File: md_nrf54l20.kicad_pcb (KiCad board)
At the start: 4 copper layers, 43.2 x 17.8 mm, 56 parts, among them J10 Conn_01x15, J2 Conn_01x04, J5 USB_C, J7 JST SH I2C, J9 Conn_01x15, SW1 RESET, U1 nRF54L20, U3 CH347T, U4 AP2112K-3.3, U5 MLD-TF PUSH-H18, U6 CH347F, Y1 8MHz, Y2 32MHz

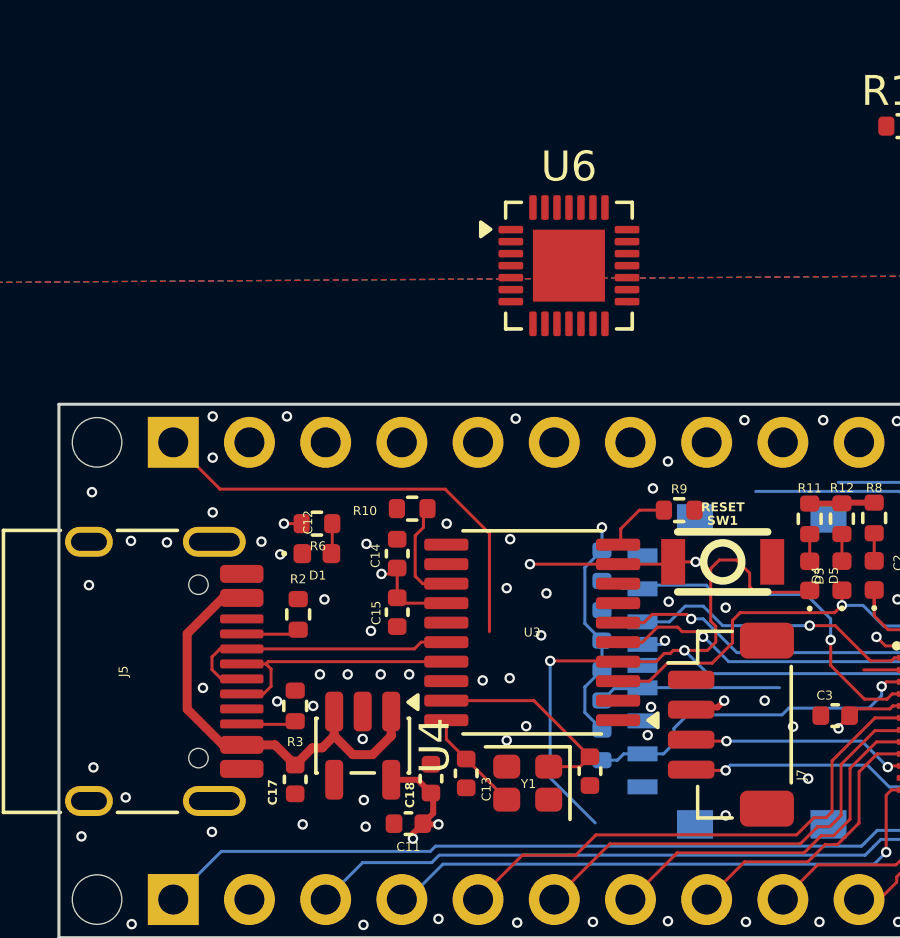
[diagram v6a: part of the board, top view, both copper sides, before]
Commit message: Swapping from ch347t to ch347f
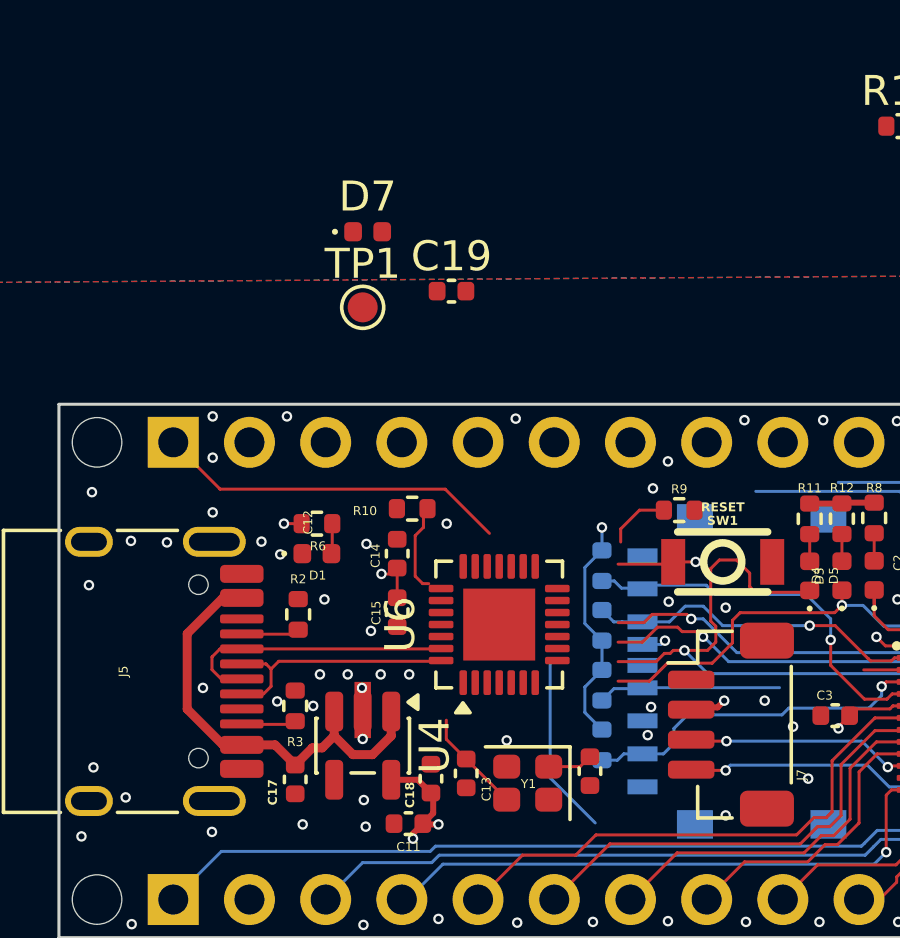
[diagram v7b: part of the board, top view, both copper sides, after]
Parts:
- removed U3: CH347T, Package_SO:TSSOP-20_4.4x6.5mm_P0.65mm
- added C19: 100nF, Capacitor_SMD:C_0402_1005Metric, F.Cu at (113.1, 78.5)
- added D7: G_LED, LED_SMD:LED_0402_1005Metric, F.Cu at (110.3, 76.5)
- added TP1: WCH_RST, TestPoint:TestPoint_Pad_D1.0mm, F.Cu at (110.1, 79.0)
- C15: value 1uF -> 100nF
- D5: value O_LED -> G_LED
- R10: value 10k -> 4.7k
- R11, R12: value 220 -> 10k
- moved U6 12.2 mm to (114.7, 89.6), turned to 90 degrees
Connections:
- C12 pad 1: Net-(U3-XI) -> Net-(U6-XI)
- C13 pad 1: Net-(U3-XO) -> Net-(U6-XO)
- D4 pad 1: /CH_UART_TX -> /nRESET
- J5 pad A6: /USB_DP -> Net-(U6-UD+)
- J5 pad A7: /USB_DN -> Net-(U6-UD-)
- J5 pad B6: /USB_DP -> Net-(U6-UD+)
- J5 pad B7: /USB_DN -> Net-(U6-UD-)
- R10 pad 1: /MODE_R -> +3V3
- R10 pad 2: GND -> Net-(U6-~{RST})
- R12 pad 1: Net-(D4-A) -> Net-(D7-A)
- R9 pad 1: /MODE_D -> Net-(D4-A)
- R9 pad 2: GND -> +3V3
- U6 pad 1: unconnected-(U6-XI-Pad1) -> Net-(U6-XI)
- U6 pad 19: unconnected-(U6-TXD0-Pad19) -> /CH_UART_TX
- U6 pad 2: unconnected-(U6-XO-Pad2) -> Net-(U6-XO)
- U6 pad 20: unconnected-(U6-GND-Pad20) -> GND
- U6 pad 21: unconnected-(U6-VCC-Pad21) -> +3V3
- U6 pad 22: unconnected-(U6-RXD0-Pad22) -> /CH_UART_RX
- U6 pad 23: unconnected-(U6-TCK/SWDCLK/GPIO4-Pad23) -> /SWDCLK
- U6 pad 26: unconnected-(U6-TMS/SWDIO/GPIO7-Pad26) -> /SWDIO
- U6 pad 27: unconnected-(U6-UD--Pad27) -> Net-(U6-UD-)
- U6 pad 28: unconnected-(U6-UD+-Pad28) -> Net-(U6-UD+)
- U6 pad 29: unconnected-(U6-GND-Pad29) -> GND
- U6 pad 3: unconnected-(U6-~{RST}-Pad3) -> Net-(U6-~{RST})
- U6 pad 6: unconnected-(U6-VIO-Pad6) -> +3V3
- U6 pad 8: unconnected-(U6-ACT/SRST-Pad8) -> /nRESET
- Y1 pad 1: Net-(U3-XI) -> Net-(U6-XI)
- Y1 pad 3: Net-(U3-XO) -> Net-(U6-XO)
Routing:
- net /USB_DN: track 9.56 -> 0.00 mm
- net Net-(U6-UD-): track 0.00 -> 9.30 mm
- net /USB_DP: track 8.75 -> 0.00 mm
- net Net-(U6-UD+): track 0.00 -> 8.49 mm
- net Net-(U3-XI): track 7.07 -> 0.00 mm
- net Net-(U6-XO): track 0.00 -> 3.49 mm
- net Net-(U3-XO): track 3.49 -> 0.00 mm
- net /D12_CITO: track 20.8 -> 17.5 mm
- net /nRESET: track 14.8 -> 11.9 mm, vias 2 -> 1
- net /MODE_R: track 2.72 -> 0.00 mm
- net /CH_UART_RX: track 34.4 -> 32.2 mm, vias 3 -> 2
- net Net-(D4-A): track 0.91 -> 3.02 mm
- net /MODE_D: track 2.11 -> 0.00 mm
- net Net-(U6-XI): track 0.00 -> 1.51 mm
- net +3V3: track 28.2 -> 29.3 mm
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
